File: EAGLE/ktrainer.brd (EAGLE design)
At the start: 54.6 x 55.9 mm, 10 parts

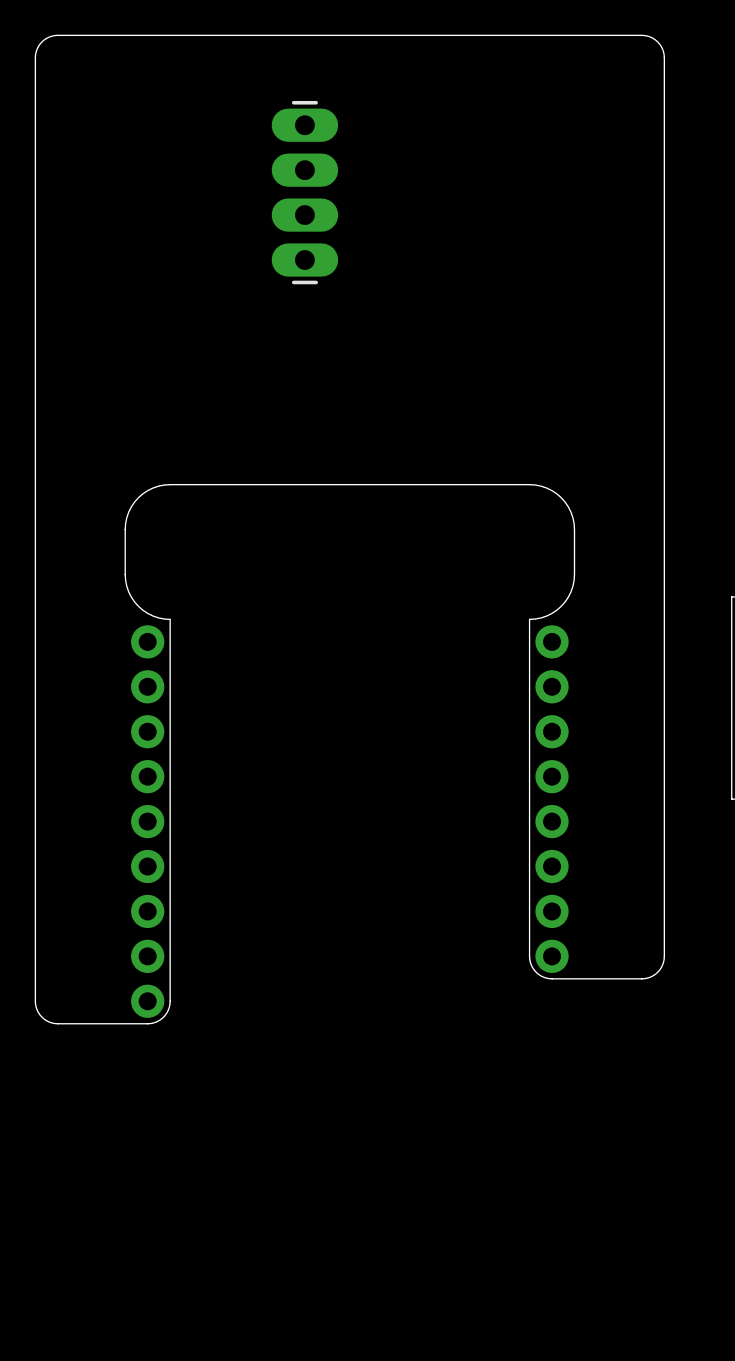
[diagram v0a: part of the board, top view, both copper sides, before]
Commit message: First thoughts on the physical layout of buttons & screen
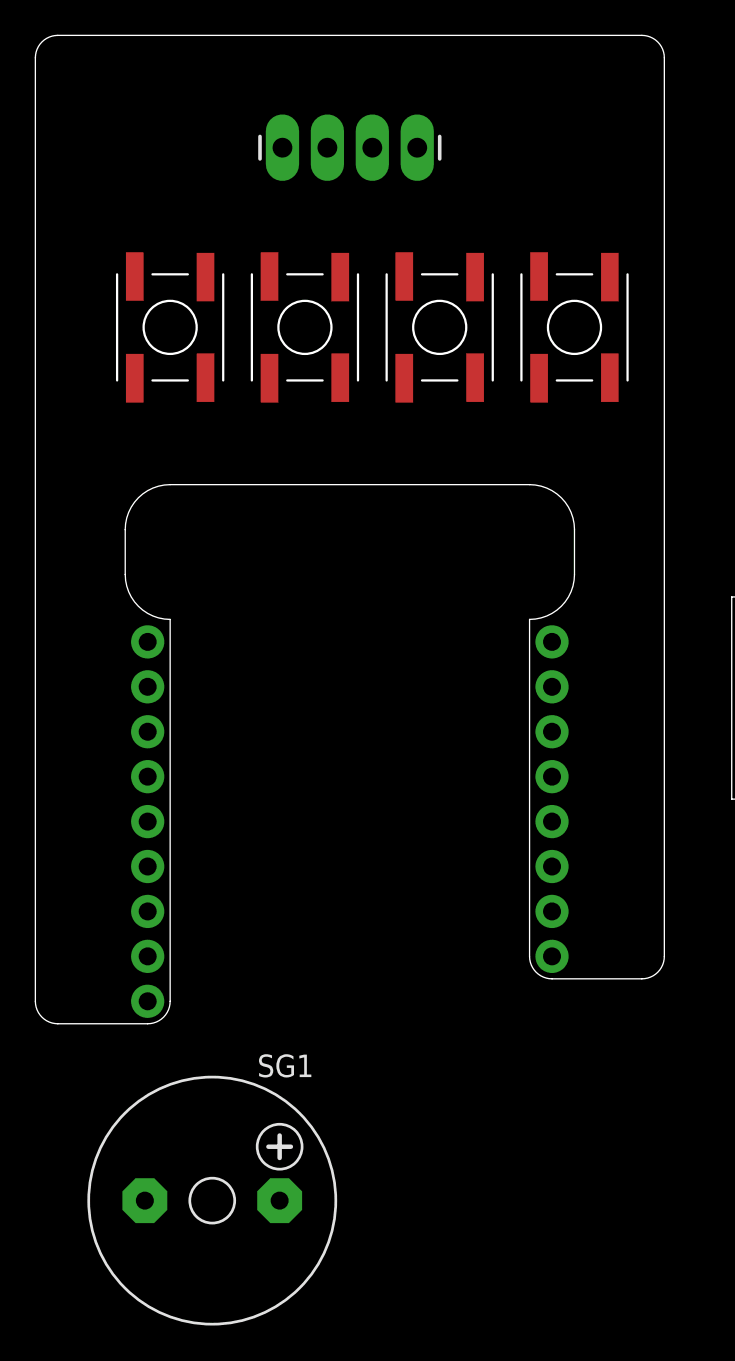
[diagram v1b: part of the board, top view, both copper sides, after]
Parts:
- added PB1, PB2, PB3, PB4: SWITCH-SKRA, formatc1702-switches:SWITCH-SKRA-PKG
- added SG1: F/CM12P, buzzer:F/CM12P
- moved JP2 6.48 mm to (21.6, 49.5), turned to 180 degrees
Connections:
- new net N$1: PB1.P$3, PB1.P$4
- new net N$2: PB2.P$3, PB2.P$4
- new net N$3: PB3.P$3, PB3.P$4
- new net N$4: PB4.P$3, PB4.P$4
- net GND: now also PB1.P$1, PB1.P$2, PB2.P$1, PB2.P$2, PB3.P$1, PB3.P$2, PB4.P$1, PB4.P$2
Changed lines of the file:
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@@
 <?xml version="1.0" encoding="utf-8"?>
 <!DOCTYPE eagle SYSTEM "eagle.dtd">
-<eagle version="7.4.0">
+<eagle version="6.5.0">
 <drawing>
 <settings>
@@
 <setting verticaltext="up"/>
 </settings>
-<grid distance="0.05" unitdist="inch" unit="inch" style="dots" multiple="1" display="yes" altdistance="0.025" altunitdist="inch" altunit="inch"/>
+<grid distance="5" unitdist="mm" unit="mm" style="dots" multiple="1" display="yes" altdistance="1" altunitdist="mm" altunit="mm"/>
 <layers>
 <layer number="1" name="Top" color="4" fill="1" visible="yes" active="yes"/>
@@
 <layer number="35" name="tGlue" color="7" fill="4" visible="no" active="yes"/>
 <layer number="36" name="bGlue" color="7" fill="5" visible="no" active="yes"/>
-<layer number="37" name="tTest" color="7" fill="1" visible="no" active="yes"/>
+<layer number="37" name="tTest" color="7" fill="1" visible="yes" active="yes"/>
 <layer number="38" name="bTest" color="7" fill="1" visible="no" active="yes"/>
 <layer number="39" name="tKeepout" color="4" fill="11" visible="yes" active="yes"/>
@@
 <wire x1="54.61" y1="12.7" x2="39.37" y2="12.7" width="0" layer="20"/>
 <wire x1="39.37" y1="12.7" x2="39.37" y2="24.13" width="0" layer="20"/>
+<wire x1="0" y1="0" x2="55" y2="0" width="0.4064" layer="37"/>
+<wire x1="55" y1="0" x2="55" y2="85" width="0.4064" layer="37"/>
+<wire x1="55" y1="85" x2="0" y2="85" width="0.4064" layer="37"/>
+<wire x1="0" y1="85" x2="0" y2="0" width="0.4064" layer="37"/>
 </plain>
 <attributes>
@@
 <pass name="Default">
 <param name="RoutingGrid" value="50mil"/>
-<param name="AutoGrid" value="1"/>
-<param name="Efforts" value="0"/>
-<param name="TopRouterVariant" value="1"/>
 <param name="tpViaShape" value="round"/>
-<param name="PrefDir.1" value="a"/>
+<param name="PrefDir.1" value="|"/>
 <param name="PrefDir.2" value="0"/>
 <param name="PrefDir.3" value="0"/>
@@
 <param name="PrefDir.14" value="0"/>
 <param name="PrefDir.15" value="0"/>
-<param name="PrefDir.16" value="a"/>
+<param name="PrefDir.16" value="-"/>
 <param name="cfVia" value="8"/>
 <param name="cfNonPref" value="5"/>
@@
 <attribute name="VALUE" x="3.175" y="22.86" size="1.27" layer="27" rot="R270"/>
 </element>
-<element name="JP2" library="SparkFun-Connectors" package="1X04_LONGPADS" value="OLED" x="15.24" y="50.8" smashed="yes" rot="R270"/>
+<element name="JP2" library="SparkFun-Connectors" package="1X04_LONGPADS" value="OLED" x="21.59" y="49.53" smashed="yes" rot="R180"/>
 <element name="JP3" library="SparkFun-Connectors" package="1X01NS-KIT" value="" x="40.64" y="10.16"/>
 <element name="JP4" library="SparkFun-Connectors" package="1X01NS-KIT" value="" x="53.34" y="10.16"/>
@@
 <element name="JP8" library="SparkFun-Connectors" package="1X01NS-KIT" value="" x="49.53" y="26.67"/>
 <element name="JP9" library="SparkFun-Connectors" package="1X01NS-KIT" value="" x="6.35" y="1.27"/>
+<element name="PB1" library="formatc1702-switches" package="SWITCH-SKRA-PKG" value="SWITCH-SKRA" x="7.62" y="39.37" rot="R90"/>
+<element name="PB2" library="formatc1702-switches" package="SWITCH-SKRA-PKG" value="SWITCH-SKRA" x="15.24" y="39.37" rot="R90"/>
+<element name="PB3" library="formatc1702-switches" package="SWITCH-SKRA-PKG" value="SWITCH-SKRA" x="22.86" y="39.37" rot="R90"/>
+<element name="PB4" library="formatc1702-switches" package="SWITCH-SKRA-PKG" value="SWITCH-SKRA" x="30.48" y="39.37" rot="R90"/>
+<element name="SG1" library="buzzer" package="F/CM12P" value="F/CM12P" x="10" y="-10">
+<attribute name="OC_NEWARK" value="unknown" x="10" y="-10" size="1.778" layer="27" display="off"/>
+<attribute name="MPN" value="" x="10" y="-10" size="1.778" layer="27" display="off"/>
+<attribute name="MF" value="" x="10" y="-10" size="1.778" layer="27" display="off"/>
+<attribute name="OC_FARNELL" value="unknown" x="10" y="-10" size="1.778" layer="27" display="off"/>
+</element>
 </elements>
 <signals>
@@
 <signal name="GND">
 <contactref element="JP1_1" pad="7"/>
+<contactref element="PB1" pad="P$1"/>
+<contactref element="PB2" pad="P$1"/>
+<contactref element="PB3" pad="P$1"/>
+<contactref element="PB4" pad="P$1"/>
+<contactref element="PB1" pad="P$2"/>
+<contactref element="PB2" pad="P$2"/>
+<contactref element="PB3" pad="P$2"/>
+<contactref element="PB4" pad="P$2"/>
+<wire x1="28.48" y1="42.245" x2="28.48" y2="36.495" width="0" layer="19" extent="1-1"/>
+<wire x1="20.86" y1="36.495" x2="28.48" y2="36.495" width="0" layer="19" extent="1-1"/>
+<wire x1="20.86" y1="42.245" x2="20.86" y2="36.495" width="0" layer="19" extent="1-1"/>
+<wire x1="13.24" y1="36.495" x2="20.86" y2="36.495" width="0" layer="19" extent="1-1"/>
+<wire x1="13.24" y1="42.245" x2="13.24" y2="36.495" width="0" layer="19" extent="1-1"/>
+<wire x1="5.62" y1="42.245" x2="13.24" y2="42.245" width="0" layer="19" extent="1-1"/>
+<wire x1="5.62" y1="36.495" x2="5.62" y2="42.245" width="0" layer="19" extent="1-1"/>
+<wire x1="6.35" y1="6.35" x2="5.62" y2="42.245" width="0" layer="19" extent="1-1"/>
 </signal>
 <signal name="D4">
@@
 <contactref element="JP9" pad="1"/>
 </signal>
+<signal name="N$1">
+<contactref element="PB1" pad="P$3"/>
+<contactref element="PB1" pad="P$4"/>
+<wire x1="9.62" y1="42.21" x2="9.62" y2="36.53" width="0" layer="19" extent="1-1"/>
+</signal>
+<signal name="N$2">
+<contactref element="PB2" pad="P$3"/>
+<contactref element="PB2" pad="P$4"/>
+<wire x1="17.24" y1="42.21" x2="17.24" y2="36.53" width="0" layer="19" extent="1-1"/>
+</signal>
+<signal name="N$3">
+<contactref element="PB3" pad="P$3"/>
+<contactref element="PB3" pad="P$4"/>
+<wire x1="24.86" y1="42.21" x2="24.86" y2="36.53" width="0" layer="19" extent="1-1"/>
+</signal>
+<signal name="N$4">
+<contactref element="PB4" pad="P$3"/>
+<contactref element="PB4" pad="P$4"/>
+<wire x1="32.48" y1="42.21" x2="32.48" y2="36.53" width="0" layer="19" extent="1-1"/>
+</signal>
 </signals>

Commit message: Work on schematic/PCB (not finished)
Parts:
- removed JP1_1: (no value), SparkFun-Connectors:1X08_NO_SILK
- removed JP2: OLED, SparkFun-Connectors:1X04_LONGPADS
- removed JP3, JP4, JP5, JP6, JP7, JP8, JP9: (no value), SparkFun-Connectors:1X01NS-KIT
- removed SG1: F/CM12P, buzzer:F/CM12P
- added BUZ1: F/CM12P, buzzer:F/CM12P
- added C1, C2: (no value), rcl:C0805
- added H1, H2, H3, H4: MOUNT-HOLE2.8, holes:2,8
- added IC1: DS3231/SO, adafruit:SO16W
- added JP10: POLOLU step up/down 3V3, SparkFun-Connectors:1X04_LONGPADS
- added LED1: WS2812B, WS2812B:WS2812B
- added R1, R2: (no value), rcl:R0805
- added S1: (no value), adafruit:EG1218
- added SJ1: (no value), jumper:SJ_2
- added U$1: TP4056-LIPO-CHG-PCB, formatc1702-pcbs:TP4056-LIPO-CHG-PCB-PACKAGE
- added U$2: SSD1306-OLED-128X64-I2C, formatc1702-pcbs:SSD1306-OLED-128X64-I2C-PACKAGE
- added UC1: Wemos D1 mini Pro, esp8266modules:WEMOS-D1-MINI
- JP1: value Wemos D1 mini pro -> (none); device SparkFun-Connectors:1X08_NO_SILK -> pinhead:1X02
- moved JP1 73.1 mm to (45.6, 75.1), turned to 0 degrees
- moved PB3 9.67 mm to (31.8, 43.2)
- moved PB4 9.67 mm to (39.4, 43.2)
- moved PB1 5.39 mm to (11.4, 43.2)
- moved PB2 5.39 mm to (19.1, 43.2)
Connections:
- removed net 3V3: JP1.1
- removed net 5V_USB: JP9.1
- removed net A0: JP1.7
- removed net D0: JP1.6
- removed net D1: JP1_1.3
- removed net D2: JP1_1.4
- removed net D3: JP1_1.5
- removed net D4: JP1_1.6
- removed net D5: JP1.5
- removed net D6: JP1.4
- removed net D7: JP1.3
- removed net D8: JP1.2
- removed net N$1: PB1.P$3, PB1.P$4
- removed net N$2: PB2.P$3, PB2.P$4
- removed net N$3: PB3.P$3, PB3.P$4
- removed net N$4: PB4.P$3, PB4.P$4
- removed net RST: JP1.8
- removed net RX: JP1_1.2
- removed net TX: JP1_1.1
- removed net V_IN: JP1_1.8
- new net +3V3: C1.1, IC1.2, JP10.1, LED1.VDD, U$2.VCC, UC1.3V3
- new net +5V: U$1.IN+, UC1.5V
- new net BATSENS: R1.1, R2.2, UC1.A0
- new net BUZZER: BUZ1.+, UC1.D7
- new net LED: LED1.DIN, UC1.D6
- new net N$5: JP1.1, U$1.B+
- new net N$6: JP1.2, U$1.B-
- new net N$7: C2.1, IC1.14, SJ1.2
- new net N$8: JP10.3, S1.S
- new net PB1: PB1.P$3, PB1.P$4, UC1.D1
- new net PB2: PB2.P$3, PB2.P$4, UC1.D2
- new net PB3: PB3.P$3, PB3.P$4, UC1.D3
- new net PB4: PB4.P$3, PB4.P$4, UC1.D4
- new net SCL: IC1.16, U$2.SCL, UC1.D5
- new net SDA: IC1.15, U$2.SDA, UC1.D0
- new net SHDN: JP10.4
- new net VCC: R1.2, S1.P, U$1.OUT+
- net GND: now also BUZ1.-, C1.2, C2.2, IC1.13, JP10.2, LED1.VSS, R2.1, SJ1.3, U$1.IN-, U$1.OUT-, U$2.GND, UC1.GND; no longer JP1_1.7
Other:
- board size 54.6 x 55.9 mm -> 49.5 x 80 mm

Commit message: More work on schematic/PCB (not finished)
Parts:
- removed BUZ1: F/CM12P, buzzer:F/CM12P
- removed H1, H2, H3, H4: MOUNT-HOLE2.8, holes:2,8
- removed JP10: POLOLU step up/down 3V3, SparkFun-Connectors:1X04_LONGPADS
- added BUZ+, BUZ-: (no value), wirepad:SMD1,27-2,54
- added JP2: (no value), pinhead:1X02
- added U$3: POLOLU-S7V8F3-3V3-STEP-UP-DOWN, formatc1702-pcbs:POLOLU-S7V8F3-3V3-STEP-UP-DOWN-PACKAGE
- C1, C2: value (none) -> 100n
- S1: device adafruit:EG1218 -> formatc1702-switches:SWITCH-MSK12D04-SLIDER-SMD-PKG
- moved S1 42.2 mm to (41.9, 59.7), turned to 270 degrees
- moved C2 17.7 mm to (16.3, 68.0), turned to 270 degrees
- moved IC1 13.0 mm to (22.9, 71.1)
- moved JP1 11.4 mm to (34.8, 71.7), turned to 90 degrees
- moved R1 9.49 mm to (6.82, 45.6), turned to 90 degrees
- moved SJ1 8.35 mm to (37.6, 66.0), turned to 90 degrees
- moved R2 8.25 mm to (6.74, 40.6), turned to 90 degrees
- moved C1 7.31 mm to (29.5, 70.4), turned to 90 degrees
- moved UC1 0.63 mm to (14.6, 19.1)
- moved U$1 0.63 mm to (38.7, 14.0)
- turned LED1 to 270 degrees
- turned PB2 to 270 degrees
- turned PB4 to 270 degrees
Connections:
- net N$7 renamed VBAT
- removed net BUZZER: BUZ1.+, UC1.D7
- removed net N$5: JP1.1, U$1.B+
- removed net SHDN: JP10.4
- new net AUX: JP2.1, UC1.D1
- new net BUZ: BUZ+.1, UC1.D0
- net +3V3: now also U$3.VOUT; no longer JP10.1
- net GND: now also BUZ-.1, JP2.2, U$3.GND; no longer BUZ1.-, JP10.2
- net LED: now also UC1.D4; no longer UC1.D6
- net N$8: now also S1.O, U$3.SHDN, U$3.VIN; no longer JP10.3, S1.S
- net PB1: now also UC1.D7; no longer UC1.D1
- net PB2: now also UC1.D8; no longer UC1.D2
- net PB4: now also UC1.D2; no longer UC1.D4
- net SCL: now also UC1.D6; no longer UC1.D5
- net SDA: now also UC1.D5; no longer UC1.D0
- net VCC: now also JP1.1, SJ1.1, U$1.B+
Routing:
- net +3V3: track 0.00 -> 144.3 mm
- net VCC: track 0.00 -> 94.2 mm, vias 0 -> 3
- net SCL: track 0.00 -> 64.5 mm
- net SDA: track 0.00 -> 61.5 mm
- net N$6: track 0.00 -> 54.0 mm
- net PB2: track 0.00 -> 41.7 mm
- net BUZ: track 0.00 -> 39.2 mm
- net PB3: track 0.00 -> 36.7 mm
- net N$8: track 0.00 -> 36.4 mm
- net PB1: track 0.00 -> 36.1 mm
- net PB4: track 0.00 -> 34.6 mm
- net LED: track 0.00 -> 31.2 mm
- net AUX: track 0.00 -> 29.4 mm
- net BATSENS: track 0.00 -> 28.3 mm
- net VBAT: track 0.00 -> 24.7 mm, vias 0 -> 2
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- added copper zone on layer 1, net GND
- added copper zone on layer 16, net GND
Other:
- board size 49.5 x 80 mm -> 45.7 x 80 mm
- board text added: "kTrainer PCB v1.0 2017-04 (c) Daniel Rojas"

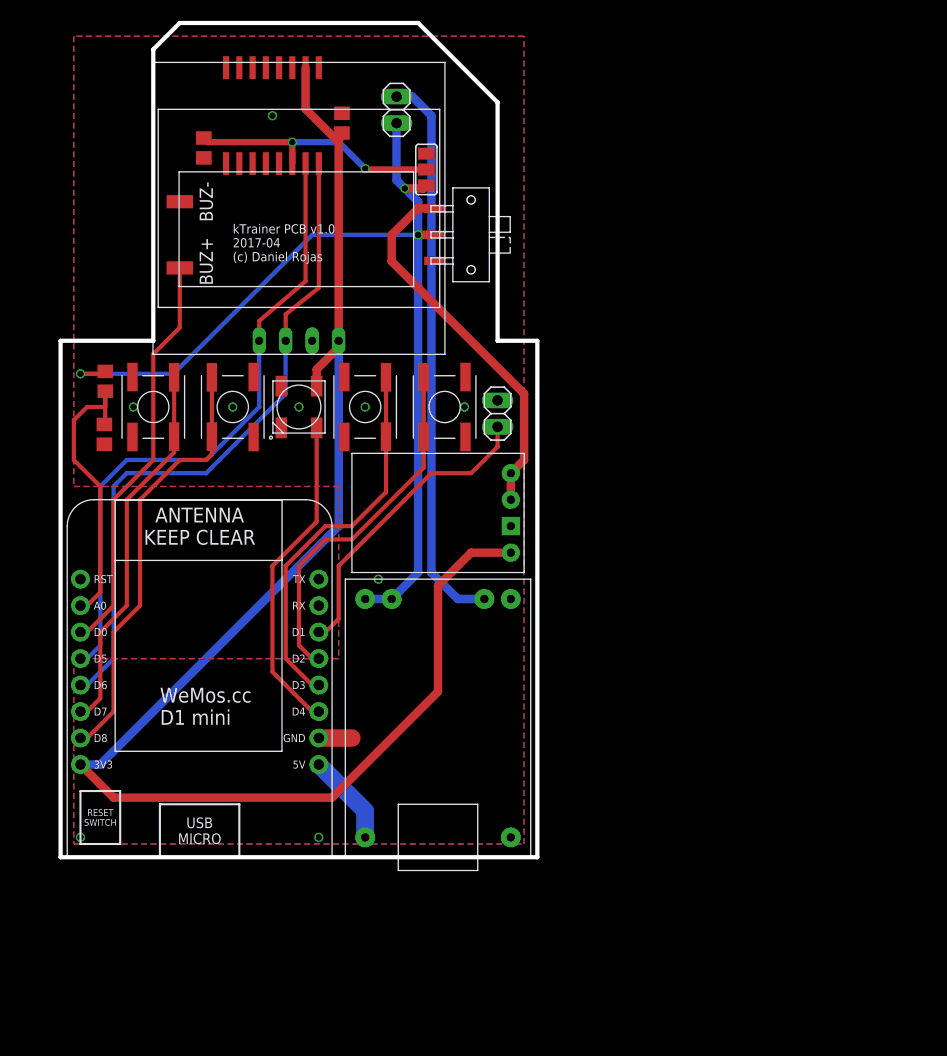
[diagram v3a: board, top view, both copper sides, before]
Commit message: Make PCB fully SMD (only vias, no through-hole pads)
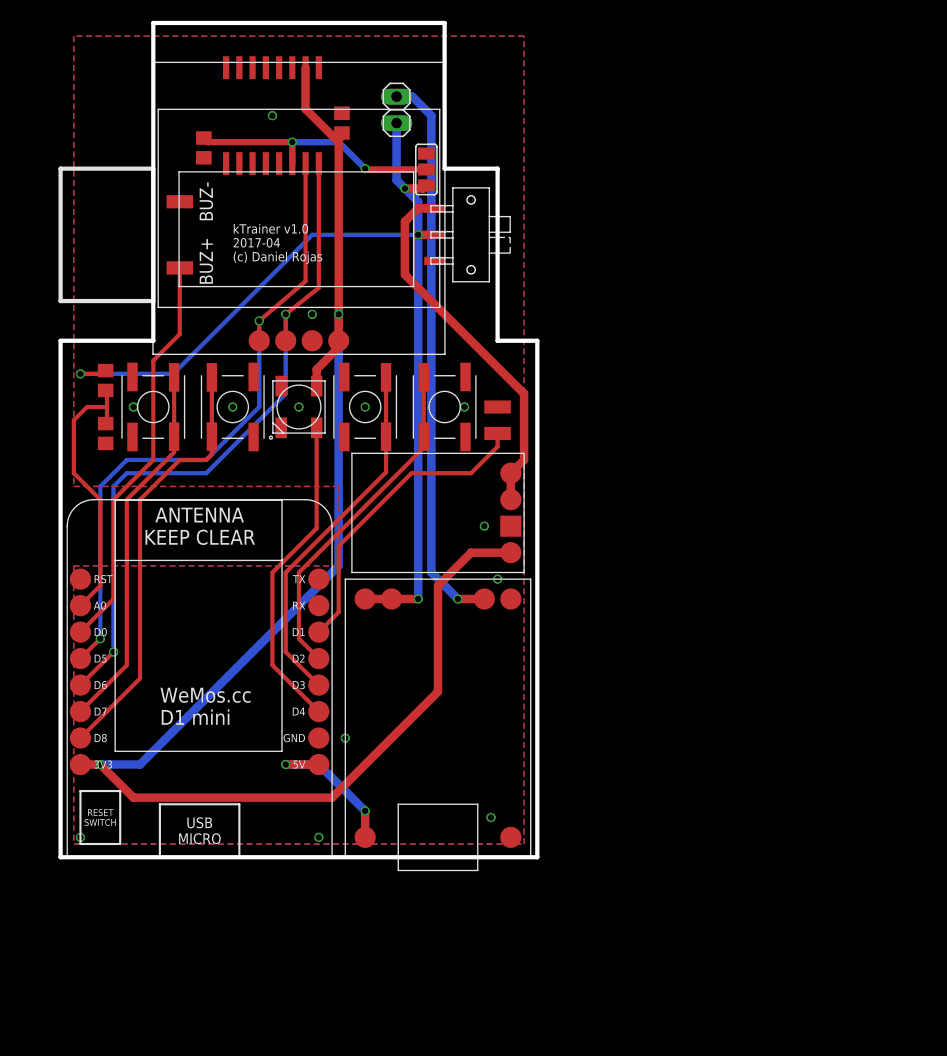
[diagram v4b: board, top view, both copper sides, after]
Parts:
- removed JP2: (no value), pinhead:1X02
- added TP-AUX, TP-AUX-GND: (no value), wirepad:SMD1,27-2,54
- U$1: value TP4056-LIPO-CHG-PCB -> TP4056-LIPO-CHG-PCBTP4056-PCB-SMD; device formatc1702-pcbs:TP4056-LIPO-CHG-PCB-PACKAGE -> formatc1702-pcbs:TP4056-PCB-SMD
- U$2: value SSD1306-OLED-128X64-I2C -> SSD1306-OLED-128X64-I2CSSD1306-OLED-128X64-SMD; device formatc1702-pcbs:SSD1306-OLED-128X64-I2C-PACKAGE -> formatc1702-pcbs:SSD1306-OLED-128X64-SMD
- U$3: value POLOLU-S7V8F3-3V3-STEP-UP-DOWN -> POLOLU-S7V8F3-3V3-STEP-UP-DOWNPOLOLU-S7V8F3-PAD; device formatc1702-pcbs:POLOLU-S7V8F3-3V3-STEP-UP-DOWN-PACKAGE -> formatc1702-pcbs:POLOLU-S7V8F3-SMD
- UC1: device esp8266modules:WEMOS-D1-MINI -> formatc1702-pcbs:WEMOS-D1-MINI-SMD
- moved UC1 2.84 mm to (15.9, 16.5)
- moved U$1 1.27 mm to (38.7, 12.7)
- moved R2 0.14 mm to (6.86, 40.6)
- moved R1 0.09 mm to (6.86, 45.7)
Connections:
- net AUX: now also TP-AUX.1; no longer JP2.1
- net GND: now also TP-AUX-GND.1; no longer JP2.2
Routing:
- net +5V: track 8.83 -> 15.2 mm, vias 0 -> 2
- net GND: track 3.18 -> 0.00 mm, vias 9 -> 13
- net +3V3: track 144.3 -> 147.2 mm, vias 0 -> 2
- net SCL: track 64.5 -> 66.7 mm, vias 0 -> 2
- net PB4: track 34.6 -> 32.8 mm
- net PB3: track 36.7 -> 34.8 mm
- net BATSENS: track 28.3 -> 26.7 mm
- net VCC: track 94.2 -> 95.8 mm, vias 3 -> 4
- net SDA: track 61.5 -> 63.0 mm, vias 0 -> 2
- net N$8: track 36.4 -> 35.3 mm
- net N$6: vias 0 -> 1
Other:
- outline, holes or cut-outs redrawn
- board text added: "kTrainer v1.0 2017-04 (c) Daniel Rojas"
- board text removed: "kTrainer PCB v1.0 2017-04 (c) Daniel Rojas"
